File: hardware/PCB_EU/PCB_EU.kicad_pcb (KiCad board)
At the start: 4 copper layers, 100 x 100 mm, 200 parts, among them J101 24 V IN, J201 UART 3V3, J301 MEM2061 SPI, J401 SHT 3V3 / GND, J402 SHT SDA / SCL, J403 FLOAT / GND, J411 FAN1: GND / +12, J412 FAN1: TACH / PWM, J421 FAN2: GND / +12, J422 FAN2: TACH / PWM, J501 LED1 + / GND, J601 LED2 + / GND, J602 BAR2 + / GND, J701 PTC + / RETURN, J702 PUMP + / RETURN, Q411 FAN1 AO3422, Q421 FAN2 AO3422, Q501 IRF540ZPBF, Q601 IRF540ZPBF, Q701 BC847B-DIO, Q702 BC857B, Q703 IRF1010ESPBF, Q704 AO3422, SW201 RESET, SW202 BOOT, U101 L7987 3A, U201 AP63203WU-7, U202 ESP32-WROOM-32E-N4, U301 MCP7940N-I/SN, U401 USBLC6-2SC6, U402 USBLC6-2SC6, U501 LM3429MH/NOPB, U601 LM3429MH/NOPB, U801 TC4427AEPA, U802 LM2903D-ST, Y301 32.768k CL7p

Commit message: hardware: apply PCB_EU review fixes
- R702 100k -> 4k7: ESP32 internal pull-up on GPIO32 (old firmware
  INPUT_PULLUP) could switch the 100 W PTC on.
- C208 100n -> 1u for the Espressif EN delay.
- Remove TC4427A driver and its parts; each LM3429 GATE drives its own
  IRF540Z through 4R7 (driver was 20-25 mm from both MOSFETs).
- Add reverse-polarity protection: Q102 IRF1010ES in the input return
  with a 5k6+5k6 / 10k gate divider.
- F103 label: UST 1206 is time-lag.
- Rebuild PCB via build_board.py + route_power.py, rerun all checks on
  KiCad 10.0.7: ERC 0, DRC 0 / parity 0, 355 unrouted, 51 checks.
- Parts estimate 80.00 -> 78.59 EUR; check ceiling raised to 100 EUR.

Co-Authored-By: Claude Opus 5.5 (1M context) <noreply@anthropic.com>
Claude-Session: https://claude.ai/code/session_01AxccZX6Cb4FnRKJMrFYMSX
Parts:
- removed C801: 10u 25V, Capacitor_SMD:C_1206_3216Metric
- removed C802: 100n, Capacitor_SMD:C_0805_2012Metric
- removed R801, R805: 1k, Resistor_SMD:R_0603_1608Metric
- removed R802, R806: 100k, Resistor_SMD:R_0603_1608Metric
- removed U801: TC4427AEPA, Package_DIP:DIP-8_W7.62mm
- added Q102: IRF1010ESPBF, Package_TO_SOT_SMD:TO-263-2, B.Cu at (10.8, 67.0)
- added R108: 5k6 1%, Resistor_SMD:R_1206_3216Metric, B.Cu at (12.3, 83.2)
- added R109: 5k6 1%, Resistor_SMD:R_1206_3216Metric, B.Cu at (12.3, 80.7)
- added R110: 10k 1%, Resistor_SMD:R_1206_3216Metric, B.Cu at (12.8, 78.2)
- C208: value 100n RESET -> 1u RESET
- F103: value 6.3 A fast -> 6.3 A slow
- R702: value 100k -> 4k7 1%; footprint Resistor_SMD:R_0603_1608Metric -> Resistor_SMD:R_1206_3216Metric
- moved R702 4.37 mm to (34.7, 91.3)
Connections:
- J101 pad 2: GND -> PSU_RTN
- R803 pad 1: LED1_TC_OUT -> LED1_GATE_RAW
- R807 pad 1: LED2_TC_OUT -> LED2_GATE_RAW

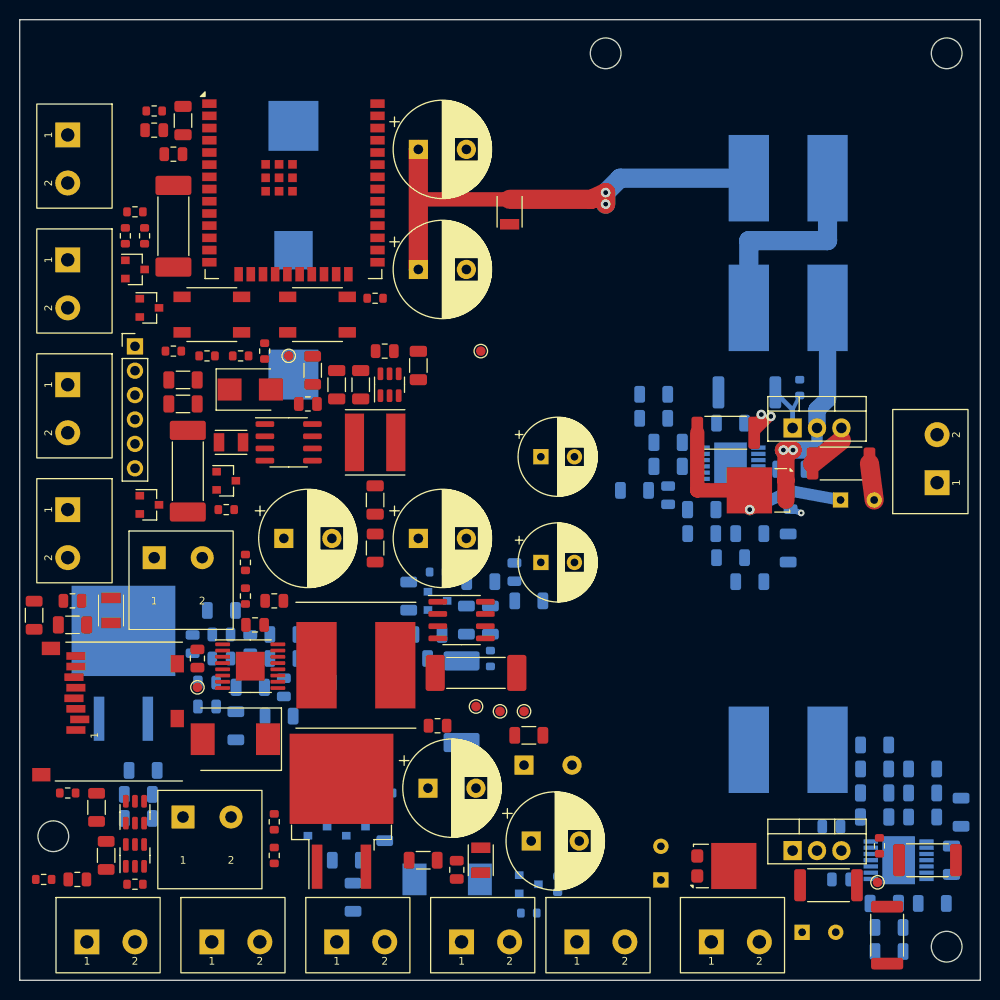
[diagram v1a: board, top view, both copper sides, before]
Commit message: PCB_EU: move BT301 away from the antenna, autoroute the board
- BT301 moved from y=24 to y=36; its courtyard is now ~12.5 mm from the
  ESP32 RF reserve (was ~2 mm).
- Net classes HEAVY24 / LOAD / PWR in PCB_EU.kicad_pro.
- tools/route_board.py: ground vias before routing (power pads, IC
  exposed pads, every SMD GND pad), grid pre-route of the LM3429/L7987
  control nets, import of two Freerouting 2.4.1 sessions (routing/),
  grid completion, GND pours on F.Cu/B.Cu, island stitching.
  Deterministic for the committed sessions.
- tools/route_complete.py: grid router adapted from hardware/route_complete.py.
- PCB_EU.kicad_dru: solid zone connection for C609.
- DRC: 0 violations, 0 parity issues, 13 unconnected (was 355).
  Open: 11 near U501/U601 between the heatsink keepouts, D101 and U101.12.
- verify_routing/run_checks report unrouted count and widths per class;
  README/DESIGN updated.

Co-Authored-By: Claude Opus 5.5 (1M context) <noreply@anthropic.com>
Claude-Session: https://claude.ai/code/session_01AxccZX6Cb4FnRKJMrFYMSX
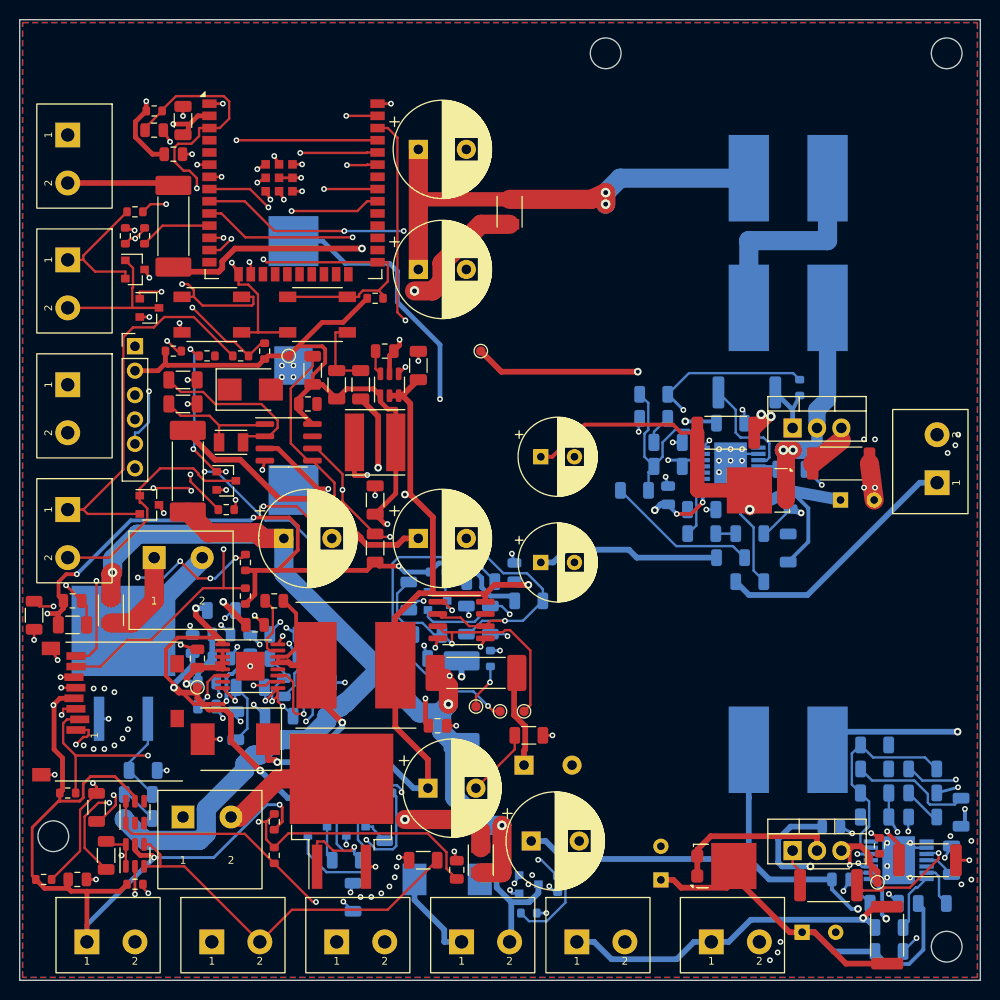
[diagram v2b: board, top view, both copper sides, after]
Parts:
- moved BT301 12.0 mm to (28.5, 36.0)
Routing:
- net +3V3: track 0.00 -> 308.0 mm, vias 0 -> 11
- net +12V: track 0.00 -> 209.8 mm, vias 0 -> 8
- net +24V_FUSED: track 0.00 -> 189.3 mm, vias 0 -> 6
- net GND: track 5.00 -> 157.8 mm, vias 1 -> 128
- net I2C_SDA: track 0.00 -> 116.5 mm, vias 0 -> 5
- net FLOAT_GPIO: track 0.00 -> 114.2 mm, vias 0 -> 2
- net PUMP_GPIO: track 0.00 -> 98.0 mm, vias 0 -> 3
- net I2C_SCL: track 0.00 -> 92.4 mm, vias 0 -> 4
- net SD_MOSI_GPIO: track 0.00 -> 88.0 mm, vias 0 -> 2
- net PTC_GPIO: track 0.00 -> 84.9 mm, vias 0 -> 4
- net +24V_AUX: track 0.00 -> 81.5 mm, vias 0 -> 2
- net LED2_SW: track 0.00 -> 75.6 mm, vias 0 -> 2
- net +24V_LED2: track 0.00 -> 75.5 mm, vias 0 -> 2
- net SD_CS: track 0.00 -> 74.4 mm, vias 0 -> 2
- net SD_MISO: track 0.00 -> 72.5 mm, vias 0 -> 2
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- added copper zone on B.Cu, net GND
- added copper zone on F.Cu, net GND
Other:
- board text added: "EU-0.1 / ROUTED, NOT RELEASED / 100 x 100 mm / 4 Cu"
- board text removed: "EU-0.1 / PARTIAL LED1 ROUTING / 100 x 100 mm / 4 Cu"
